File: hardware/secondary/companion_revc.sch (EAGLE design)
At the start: 13 parts, among them U1 USD-SOCKET

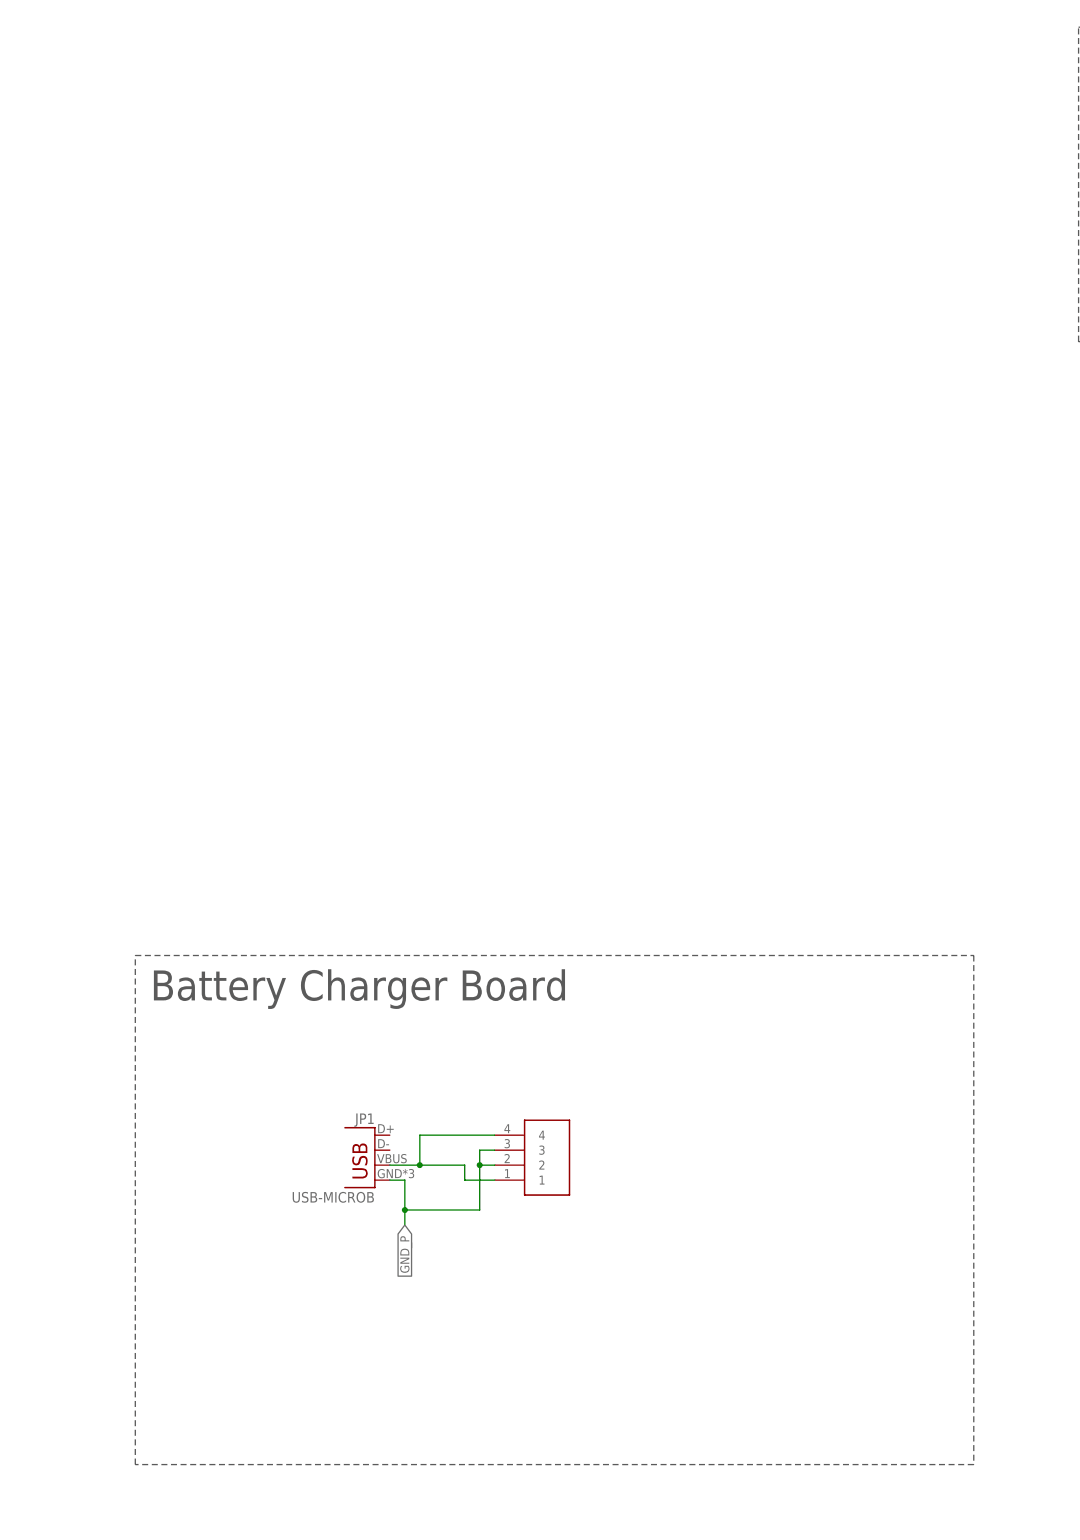
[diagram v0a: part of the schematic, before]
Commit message: Added license text to remaining files, and to CAD EAGLE schematics.
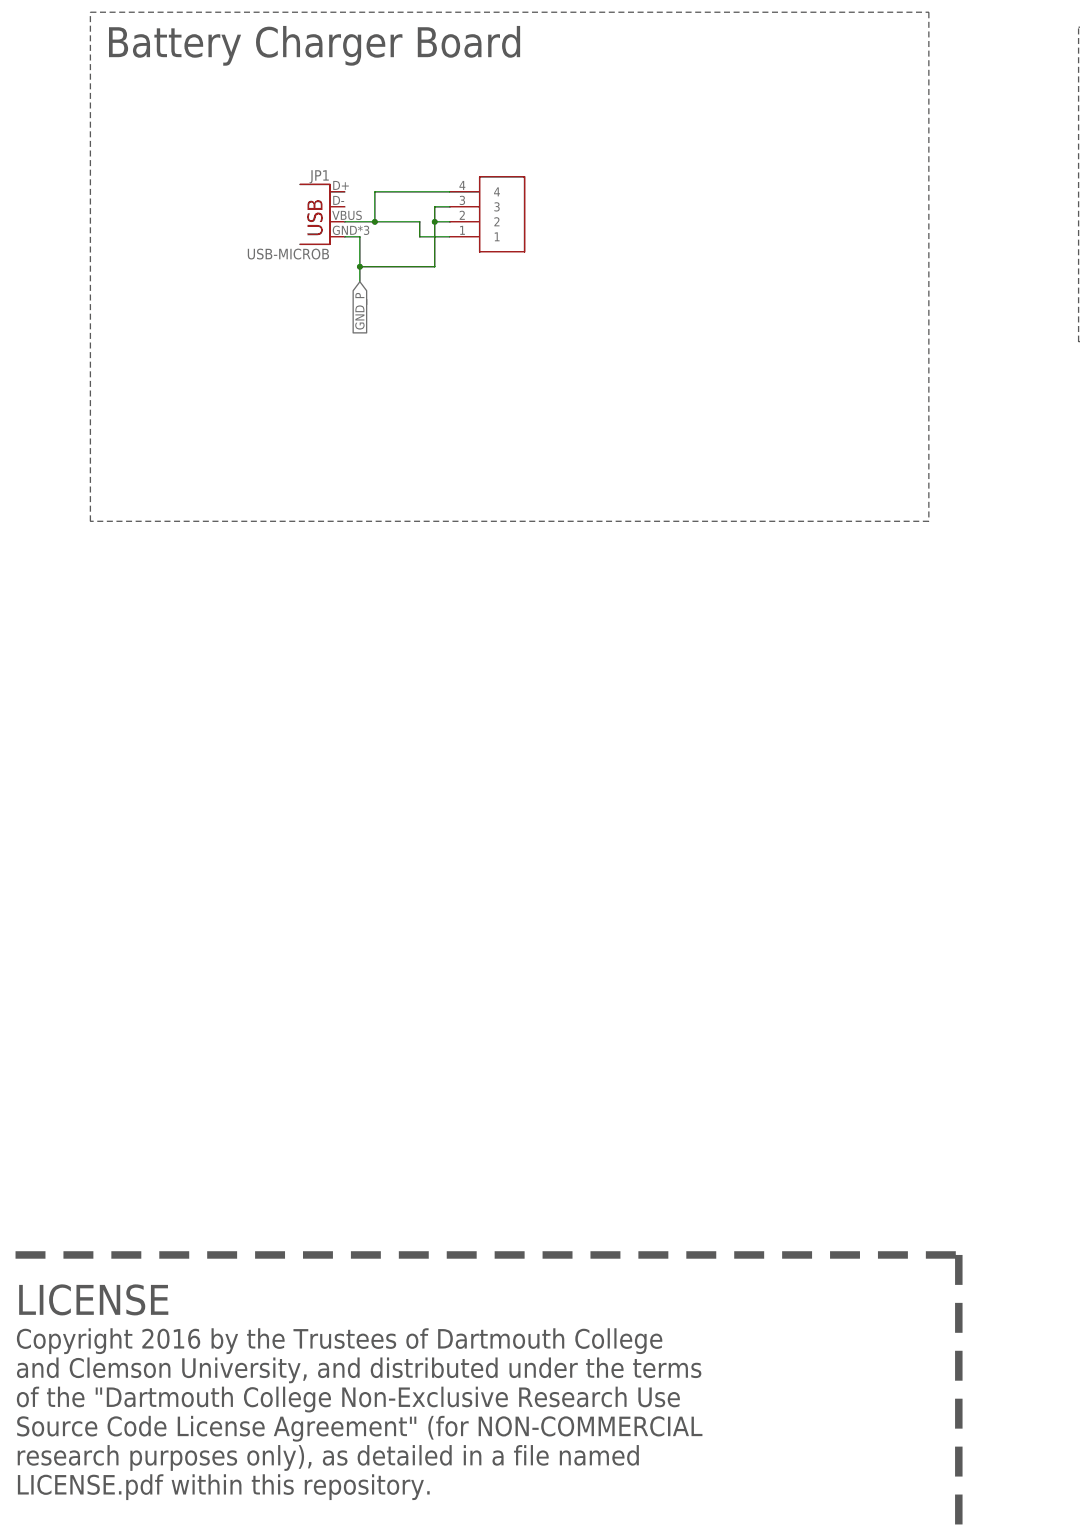
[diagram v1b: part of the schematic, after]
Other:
- note added: "Copyright 2016 by the Trustees of Dartmouth College and Clemson University, and distributed under the terms of the "Dartmouth College Non-Exclusive Research Use Source Code License Agreement" (for NON-COMMERCIAL research purposes only), as detailed in a file named LICENSE.pdf within this repository."
- note added: "LICENSE"
- moved on the sheet: JP1
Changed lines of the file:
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@@
 <text x="188.976" y="242.57" size="5.08" layer="97">Capacitive Touch
 Board</text>
-<text x="30.48" y="91.44" size="5.08" layer="97">Battery Charger Board</text>
+<text x="22.86" y="251.46" size="5.08" layer="97">Battery Charger Board</text>
 <wire x1="187.96" y1="256.54" x2="254" y2="256.54" width="0.1524" layer="97" style="longdash"/>
 <wire x1="254" y1="256.54" x2="254" y2="203.2" width="0.1524" layer="97" style="longdash"/>
@@
 <wire x1="401.32" y1="170.18" x2="218.44" y2="170.18" width="0.1524" layer="97" style="longdash"/>
 <text x="220.98" y="162.56" size="5.08" layer="97">Storage Board</text>
-<wire x1="27.94" y1="99.06" x2="170.18" y2="99.06" width="0.1524" layer="97" style="longdash"/>
-<wire x1="170.18" y1="99.06" x2="170.18" y2="12.7" width="0.1524" layer="97" style="longdash"/>
-<wire x1="170.18" y1="12.7" x2="27.94" y2="12.7" width="0.1524" layer="97" style="longdash"/>
-<wire x1="27.94" y1="12.7" x2="27.94" y2="99.06" width="0.1524" layer="97" style="longdash"/>
+<wire x1="20.32" y1="259.08" x2="162.56" y2="259.08" width="0.1524" layer="97" style="longdash"/>
+<wire x1="162.56" y1="259.08" x2="162.56" y2="172.72" width="0.1524" layer="97" style="longdash"/>
+<wire x1="162.56" y1="172.72" x2="20.32" y2="172.72" width="0.1524" layer="97" style="longdash"/>
+<wire x1="20.32" y1="172.72" x2="20.32" y2="259.08" width="0.1524" layer="97" style="longdash"/>
+<text x="7.62" y="7.62" size="3.302" layer="97" font="vector" ratio="15">Copyright 2016 by the Trustees of Dartmouth College
+and Clemson University, and distributed under the terms
+of the "Dartmouth College Non-Exclusive Research Use
+Source Code License Agreement" (for NON-COMMERCIAL
+research purposes only), as detailed in a file named
+LICENSE.pdf within this repository.</text>
+<text x="7.62" y="38.1" size="5.08" layer="97" font="vector" ratio="23">LICENSE</text>
+<wire x1="7.62" y1="48.26" x2="167.64" y2="48.26" width="1.27" layer="97" style="longdash"/>
+<wire x1="167.64" y1="48.26" x2="167.64" y2="2.54" width="1.27" layer="97" style="longdash"/>
 </plain>
 <instances>
@@
 <instance part="U$8" gate="G$1" x="238.76" y="134.62" rot="R180"/>
 <instance part="U$9" gate="G$1" x="238.76" y="127" rot="R180"/>
-<instance part="JP1" gate="G$1" x="68.58" y="60.96" rot="MR0"/>
-<instance part="U$10" gate="G$1" x="93.98" y="66.04" rot="R180"/>
+<instance part="JP1" gate="G$1" x="60.96" y="220.98" rot="MR0"/>
+<instance part="U$10" gate="G$1" x="86.36" y="226.06" rot="R180"/>
 <instance part="JP3" gate="JP1" x="309.88" y="83.82"/>
 </instances>
@@
 <segment>
 <pinref part="JP1" gate="G$1" pin="GND"/>
-<wire x1="71.12" y1="60.96" x2="73.66" y2="60.96" width="0.1524" layer="91"/>
-<label x="73.66" y="53.34" size="1.524" layer="95" rot="R270" xref="yes"/>
+<wire x1="63.5" y1="220.98" x2="66.04" y2="220.98" width="0.1524" layer="91"/>
+<label x="66.04" y="213.36" size="1.524" layer="95" rot="R270" xref="yes"/>
 <pinref part="U$10" gate="G$1" pin="3"/>
-<wire x1="88.9" y1="66.04" x2="86.36" y2="66.04" width="0.1524" layer="91"/>
-<wire x1="86.36" y1="66.04" x2="86.36" y2="63.5" width="0.1524" layer="91"/>
+<wire x1="81.28" y1="226.06" x2="78.74" y2="226.06" width="0.1524" layer="91"/>
+<wire x1="78.74" y1="226.06" x2="78.74" y2="223.52" width="0.1524" layer="91"/>
 <pinref part="U$10" gate="G$1" pin="2"/>
-<wire x1="86.36" y1="63.5" x2="88.9" y2="63.5" width="0.1524" layer="91"/>
-<wire x1="86.36" y1="63.5" x2="86.36" y2="55.88" width="0.1524" layer="91"/>
-<junction x="86.36" y="63.5"/>
-<wire x1="86.36" y1="55.88" x2="73.66" y2="55.88" width="0.1524" layer="91"/>
-<wire x1="73.66" y1="55.88" x2="73.66" y2="60.96" width="0.1524" layer="91"/>
-<wire x1="73.66" y1="53.34" x2="73.66" y2="55.88" width="0.1524" layer="91"/>
-<junction x="73.66" y="55.88"/>
+<wire x1="78.74" y1="223.52" x2="81.28" y2="223.52" width="0.1524" layer="91"/>
+<wire x1="78.74" y1="223.52" x2="78.74" y2="215.9" width="0.1524" layer="91"/>
+<junction x="78.74" y="223.52"/>
+<wire x1="78.74" y1="215.9" x2="66.04" y2="215.9" width="0.1524" layer="91"/>
+<wire x1="66.04" y1="215.9" x2="66.04" y2="220.98" width="0.1524" layer="91"/>
+<wire x1="66.04" y1="213.36" x2="66.04" y2="215.9" width="0.1524" layer="91"/>
+<junction x="66.04" y="215.9"/>
 </segment>
 </net>
@@
 <segment>
 <pinref part="JP1" gate="G$1" pin="VBUS"/>
-<wire x1="71.12" y1="63.5" x2="76.2" y2="63.5" width="0.1524" layer="91"/>
-<wire x1="76.2" y1="63.5" x2="83.82" y2="63.5" width="0.1524" layer="91"/>
-<wire x1="83.82" y1="63.5" x2="83.82" y2="60.96" width="0.1524" layer="91"/>
+<wire x1="63.5" y1="223.52" x2="68.58" y2="223.52" width="0.1524" layer="91"/>
+<wire x1="68.58" y1="223.52" x2="76.2" y2="223.52" width="0.1524" layer="91"/>
+<wire x1="76.2" y1="223.52" x2="76.2" y2="220.98" width="0.1524" layer="91"/>
 <pinref part="U$10" gate="G$1" pin="1"/>
-<wire x1="83.82" y1="60.96" x2="88.9" y2="60.96" width="0.1524" layer="91"/>
+<wire x1="76.2" y1="220.98" x2="81.28" y2="220.98" width="0.1524" layer="91"/>
 <pinref part="U$10" gate="G$1" pin="4"/>
-<wire x1="88.9" y1="68.58" x2="76.2" y2="68.58" width="0.1524" layer="91"/>
-<wire x1="76.2" y1="68.58" x2="76.2" y2="63.5" width="0.1524" layer="91"/>
-<junction x="76.2" y="63.5"/>
-</segment>
-</net>
+<wire x1="81.28" y1="228.6" x2="68.58" y2="228.6" width="0.1524" layer="91"/>
+<wire x1="68.58" y1="228.6" x2="68.58" y2="223.52" width="0.1524" layer="91"/>
+<junction x="68.58" y="223.52"/>
+</segment>
+</net>
